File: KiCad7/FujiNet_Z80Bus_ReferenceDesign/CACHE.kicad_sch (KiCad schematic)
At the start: 6 parts, among them IC1 7432N, IC10 7408N, IC11 74590N, IC12 74590N

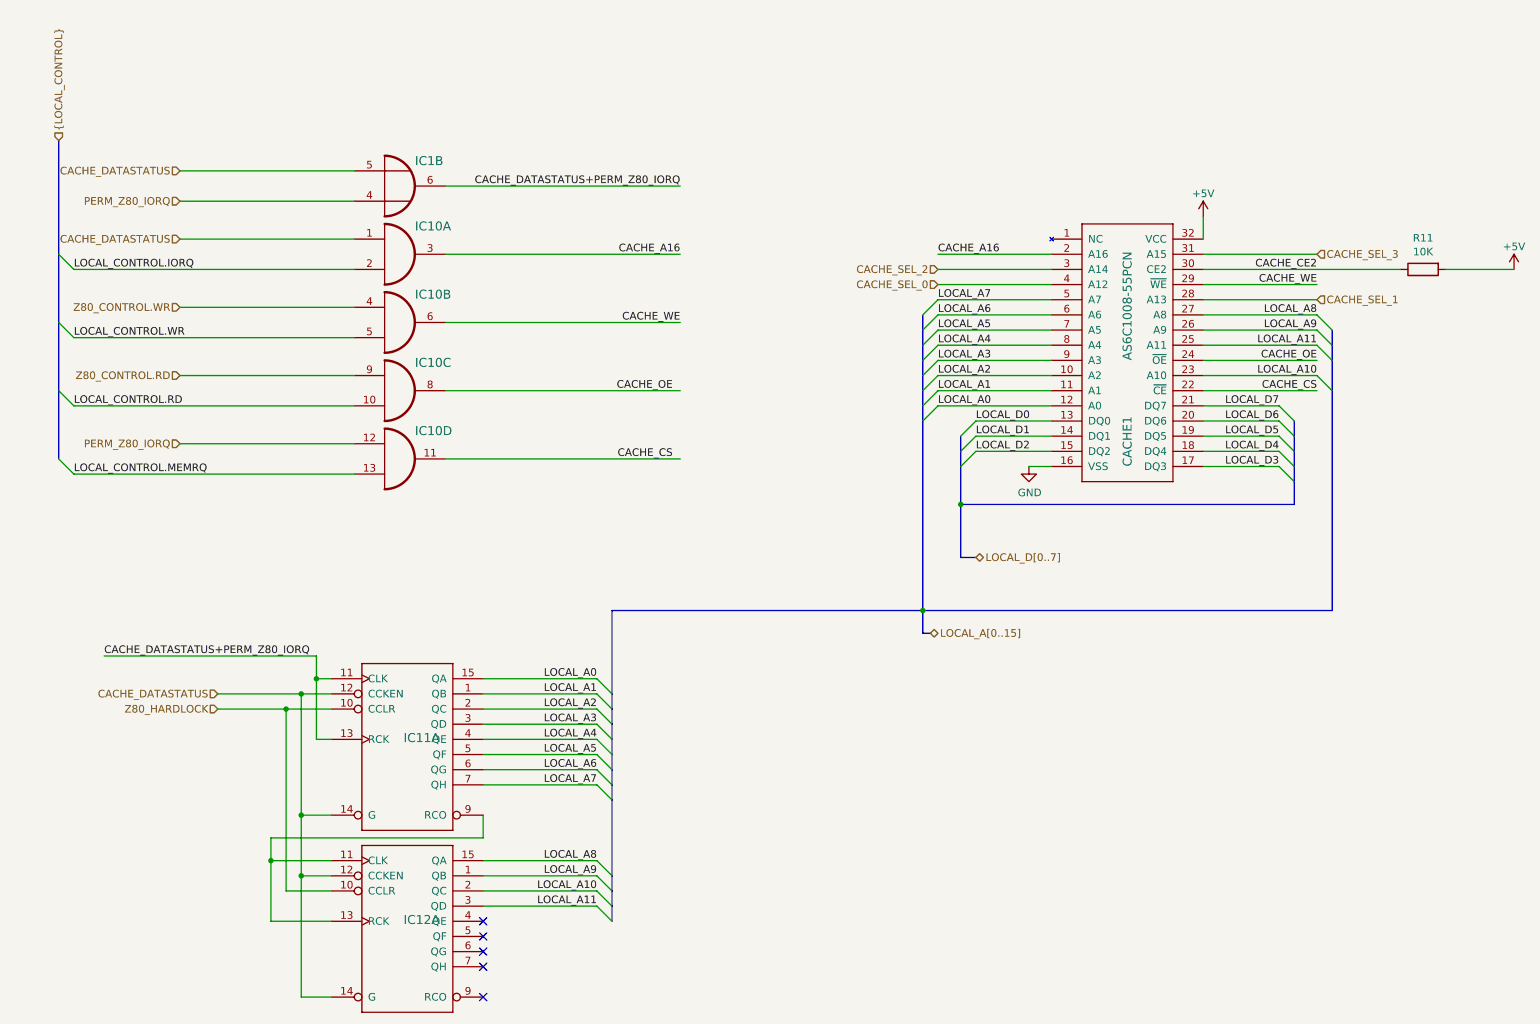
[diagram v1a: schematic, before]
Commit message: KiCad massive refactoring to enable modular PCB design
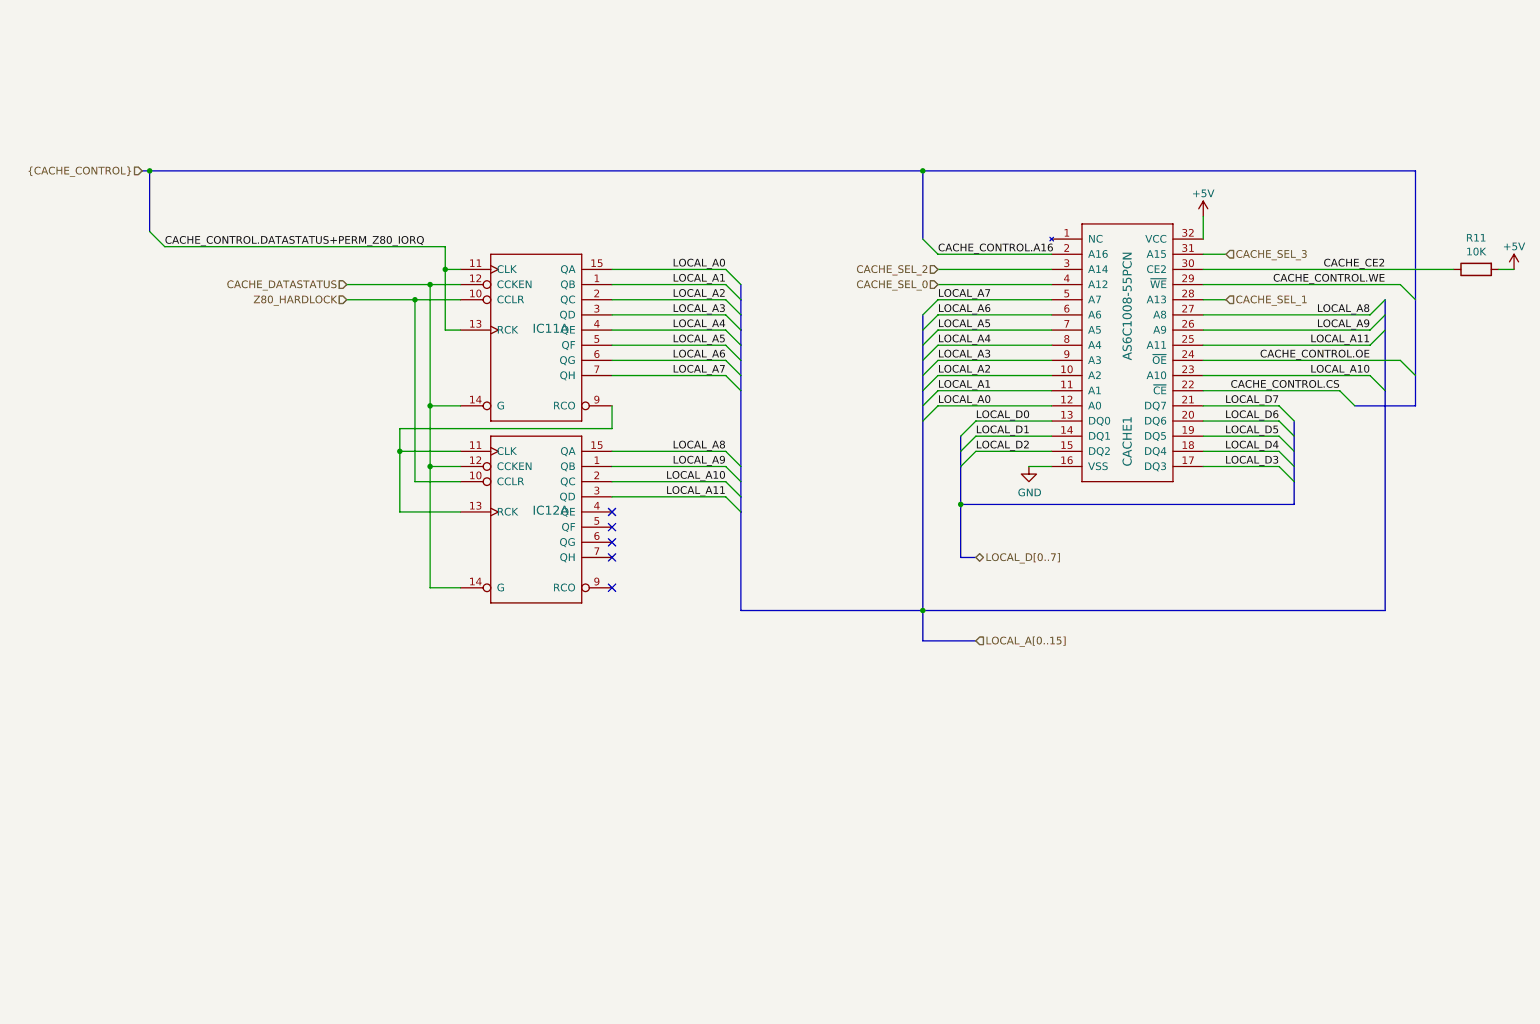
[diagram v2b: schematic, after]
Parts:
- removed IC1: 7432N, Package_DIP:DIP-14_W7.62mm_Socket, symbol FujiNet_Z80Bus_Reference-rescue:7432N-Z80ESP-eagle-import
- removed IC10: 7408N, Package_DIP:DIP-14_W7.62mm_Socket, symbol FujiNet_Z80Bus_Reference-rescue:7408N-Z80Decoder-eagle-import
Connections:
- net CACHE_A16 renamed CACHE_CONTROL.A16
- net CACHE_CS renamed CACHE_CONTROL.CS
- net CACHE_DATASTATUS+PERM_Z80_IORQ renamed CACHE_CONTROL.DATASTATUS+PERM_Z80_IORQ
- net CACHE_OE renamed CACHE_CONTROL.OE
- net CACHE_WE renamed CACHE_CONTROL.WE
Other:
- moved on the sheet: IC11A, IC12A, R11

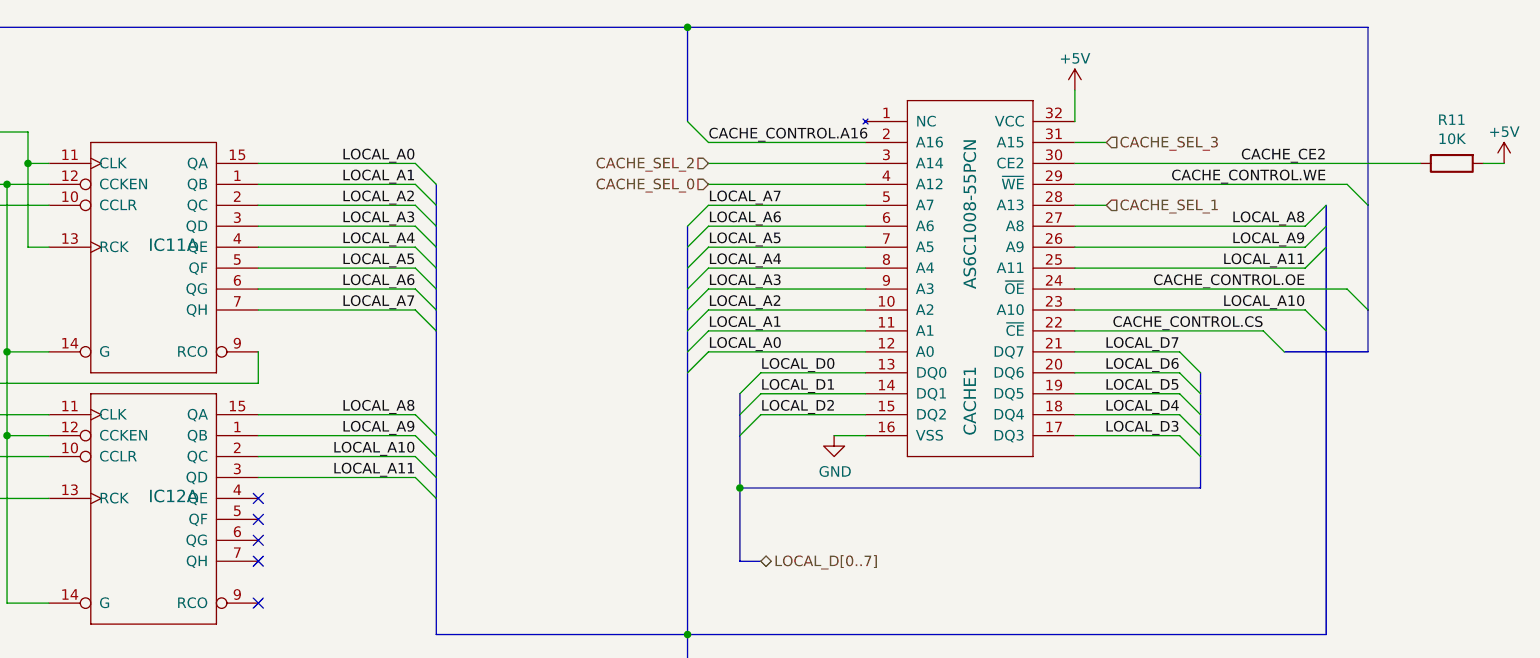
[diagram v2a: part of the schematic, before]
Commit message: Unpicked CoreLogic Buses, some symbol updates
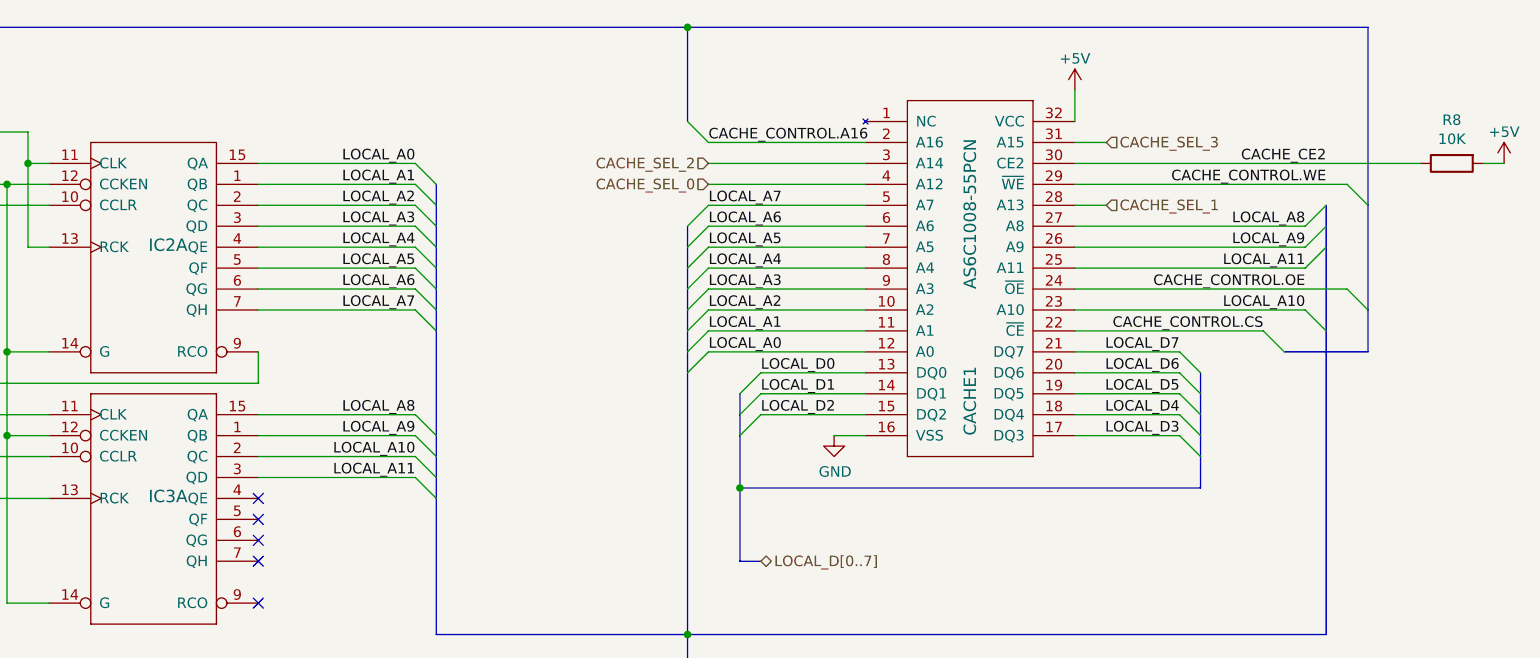
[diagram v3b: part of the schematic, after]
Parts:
- renumbered IC11 to IC2, IC12 to IC3, R11 to R8
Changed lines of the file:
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@@
   (symbol (lib_id "FujiNet_Z80Bus_Reference-rescue:74590N-Z80ESP-eagle-import") (at 111.76 100.33 0) (unit 1)
     (in_bom yes) (on_board yes) (dnp no)
-    (property "Reference" "IC12" (at 111.125 100.965 0)
+    (property "Reference" "IC3" (at 111.125 100.965 0)
       (effects (font (size 1.4986 1.4986)) (justify left bottom))
     )
@@
       (project "FujiNet_Z80Bus_ReferenceDesign"
         (path "/532c0392-800e-45cc-8170-6d32f2390e83/00000000-0000-0000-0000-0000ae2cbb6b"
-          (reference "IC12") (unit 1)
+          (reference "IC3") (unit 1)
         )
       )
@@
   (symbol (lib_id "FujiNet_Z80Bus_Reference-rescue:74590N-Z80ESP-eagle-import") (at 111.76 69.85 0) (unit 1)
     (in_bom yes) (on_board yes) (dnp no)
-    (property "Reference" "IC11" (at 111.125 70.485 0)
+    (property "Reference" "IC2" (at 111.125 70.485 0)
       (effects (font (size 1.4986 1.4986)) (justify left bottom))
     )
@@
       (project "FujiNet_Z80Bus_ReferenceDesign"
         (path "/532c0392-800e-45cc-8170-6d32f2390e83/00000000-0000-0000-0000-0000ae2cbb6b"
-          (reference "IC11") (unit 1)
+          (reference "IC2") (unit 1)
         )
         (path "/532c0392-800e-45cc-8170-6d32f2390e83"
@@
   (symbol (lib_id "Device:R") (at 269.24 59.69 90) (mirror x) (unit 1)
     (in_bom yes) (on_board yes) (dnp no)
-    (property "Reference" "R11" (at 269.24 54.4322 90)
+    (property "Reference" "R8" (at 269.24 54.4322 90)
       (effects (font (size 1.27 1.27)))
     )
@@
       (project "FujiNet_Z80Bus_ReferenceDesign"
         (path "/532c0392-800e-45cc-8170-6d32f2390e83/00000000-0000-0000-0000-0000ae2cbb6b"
-          (reference "R11") (unit 1)
+          (reference "R8") (unit 1)
         )
       )
@@
   (symbol (lib_id "power:GND") (at 194.31 92.71 0) (unit 1)
     (in_bom yes) (on_board yes) (dnp no)
-    (property "Reference" "#PWR029" (at 194.31 99.06 0)
+    (property "Reference" "#PWR024" (at 194.31 99.06 0)
       (effects (font (size 1.27 1.27)) hide)
     )
@@
       (project "FujiNet_Z80Bus_ReferenceDesign"
         (path "/532c0392-800e-45cc-8170-6d32f2390e83/00000000-0000-0000-0000-0000ae2cbb6b"
-          (reference "#PWR029") (unit 1)
+          (reference "#PWR024") (unit 1)
         )
       )
@@
   (symbol (lib_id "power:+5V") (at 223.52 50.8 0) (unit 1)
     (in_bom yes) (on_board yes) (dnp no) (fields_autoplaced)
-    (property "Reference" "#PWR030" (at 223.52 54.61 0)
+    (property "Reference" "#PWR025" (at 223.52 54.61 0)
       (effects (font (size 1.27 1.27)) hide)
     )
@@
       (project "FujiNet_Z80Bus_ReferenceDesign"
         (path "/532c0392-800e-45cc-8170-6d32f2390e83/00000000-0000-0000-0000-0000ae2cbb6b"
-          (reference "#PWR030") (unit 1)
+          (reference "#PWR025") (unit 1)
         )
       )
@@
   (symbol (lib_id "power:+5V") (at 275.59 59.69 0) (mirror y) (unit 1)
     (in_bom yes) (on_board yes) (dnp no) (fields_autoplaced)
-    (property "Reference" "#PWR031" (at 275.59 63.5 0)
+    (property "Reference" "#PWR026" (at 275.59 63.5 0)
       (effects (font (size 1.27 1.27)) hide)
     )
@@
       (project "FujiNet_Z80Bus_ReferenceDesign"
         (path "/532c0392-800e-45cc-8170-6d32f2390e83/00000000-0000-0000-0000-0000ae2cbb6b"
-          (reference "#PWR031") (unit 1)
-        )
-      )
+          (reference "#PWR026") (unit 1)
+        )
+      )

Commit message: KiCad - ALMOST ERROR FREE!!!!
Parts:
- IC2, IC3: symbol FujiNet_Z80Bus_Reference-rescue:74590N-Z80ESP-eagle-import -> 74xx:74HC590
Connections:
- net +5V: now also IC2.16 (VCC), IC3.16 (VCC)
- net GND: now also IC2.8 (GND), IC3.8 (GND)
